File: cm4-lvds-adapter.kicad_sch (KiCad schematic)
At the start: 58 parts, among them J1 Plug_Molex_SlimStack_2x15_538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, J2 JST_SM_1x10_SM10B-SURS-TF-LF-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, J3 FFC_Amphenol_1x40_62684-40110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, U2 NTS0104_DHVQFN, U3 SN65DSI84

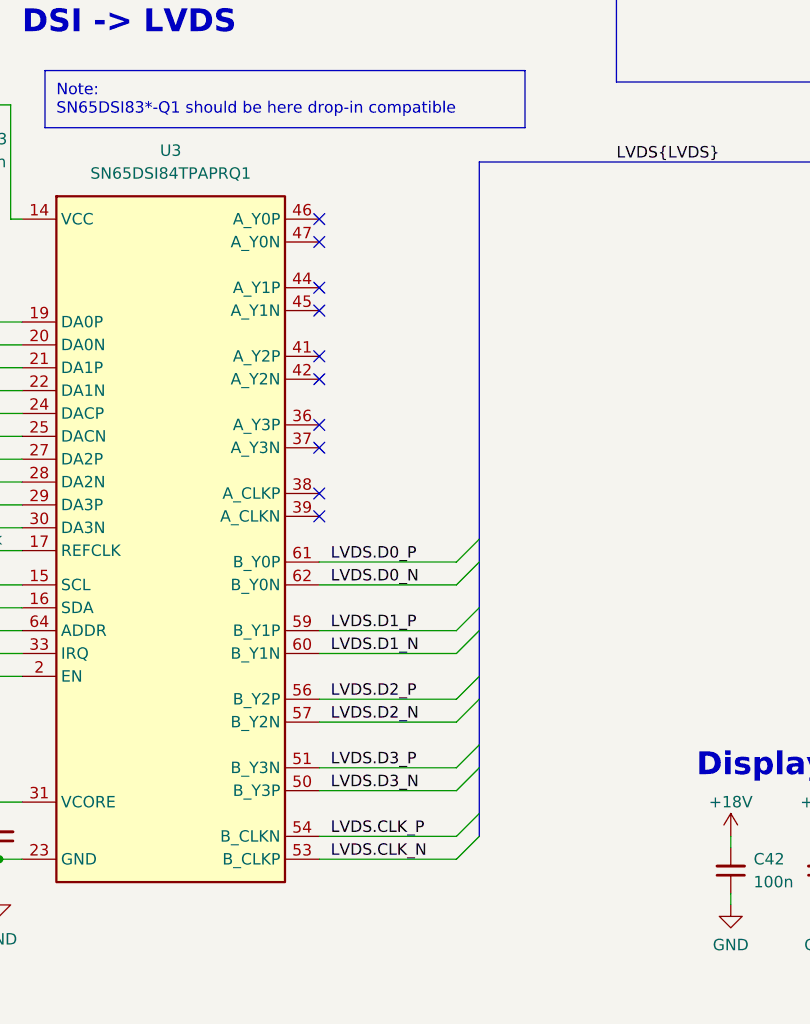
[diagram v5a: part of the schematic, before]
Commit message: [#55272] Correct pin assignment
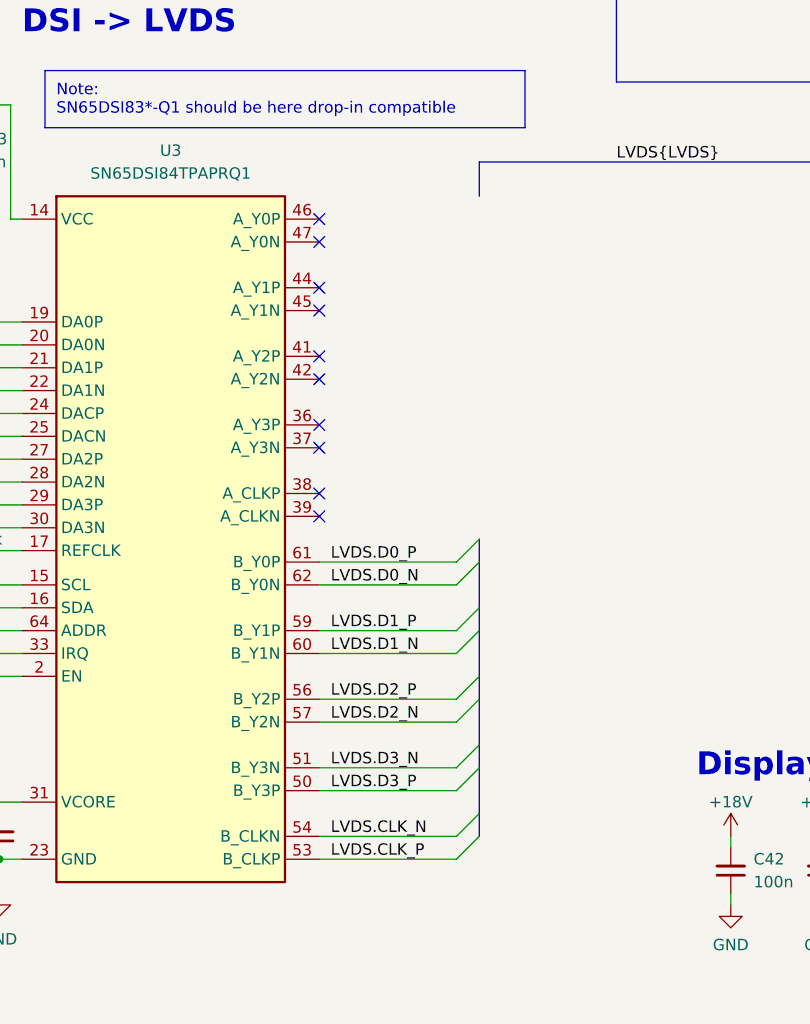
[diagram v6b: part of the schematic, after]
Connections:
- net LVDS.CLK_N: now also U3.54 (B_CLKN); no longer U3.53 (B_CLKP)
- net LVDS.CLK_P: now also U3.53 (B_CLKP); no longer U3.54 (B_CLKN)
- net LVDS.D3_N: now also U3.51 (B_Y3N); no longer U3.50 (B_Y3P)
- net LVDS.D3_P: now also U3.50 (B_Y3P); no longer U3.51 (B_Y3N)
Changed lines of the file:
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@@
     (stroke (width 0) (type default))
   )
-  (bus_entry (at 279.4 187.96) (size -2.54 2.54)
+  (bus_entry (at 279.4 185.42) (size -2.54 2.54)
     (stroke (width 0) (type default))
   )
@@
     (stroke (width 0) (type default))
   )
-  (bus_entry (at 279.4 185.42) (size -2.54 2.54)
+  (bus_entry (at 279.4 187.96) (size -2.54 2.54)
     (stroke (width 0) (type default))
   )
@@
     (stroke (width 0) (type default))
   )
+  (bus (pts (xy 279.4 185.42) (xy 279.4 187.96))
+    (stroke (width 0) (type default))
+  )
   (wire (pts (xy 100.33 189.23) (xy 120.65 189.23))
     (stroke (width 0) (type default))
@@
     (stroke (width 0) (type default))
   )
-  (bus (pts (xy 279.4 113.03) (xy 279.4 154.94))
+  (bus (pts (xy 279.4 113.03) (xy 279.4 116.84))
     (stroke (width 0) (type default))
   )
@@
     (stroke (width 0) (type default))
   )
-  (wire (pts (xy 261.62 187.96) (xy 276.86 187.96))
+  (wire (pts (xy 261.62 190.5) (xy 276.86 190.5))
     (stroke (width 0) (type default))
   )
@@
     (stroke (width 0) (type default))
   )
-  (wire (pts (xy 261.62 190.5) (xy 276.86 190.5))
+  (wire (pts (xy 261.62 187.96) (xy 276.86 187.96))
     (stroke (width 0) (type default))
   )
@@
     (stroke (width 0) (type default))
   )
-  (wire (pts (xy 261.62 182.88) (xy 276.86 182.88))
+  (wire (pts (xy 261.62 180.34) (xy 276.86 180.34))
     (stroke (width 0) (type default))
   )
@@
     (stroke (width 0) (type default))
   )
-  (bus (pts (xy 279.4 185.42) (xy 279.4 187.96))
-    (stroke (width 0) (type default))
-  )
   (wire (pts (xy 374.65 110.49) (xy 392.43 110.49))
     (stroke (width 0) (type default))
   )
-  (wire (pts (xy 261.62 180.34) (xy 276.86 180.34))
+  (wire (pts (xy 261.62 182.88) (xy 276.86 182.88))
     (stroke (width 0) (type default))
   )
@@
     (effects (font (size 1.27 1.27)) (justify right bottom))
   )
-  (label "LVDS.D3_P" (at 262.89 180.34 0) (fields_autoplaced)
+  (label "LVDS.D3_P" (at 262.89 182.88 0) (fields_autoplaced)
     (effects (font (size 1.27 1.27)) (justify left bottom))
   )
@@
     (effects (font (size 1.27 1.27)) (justify left bottom))
   )
-  (label "LVDS.CLK_P" (at 262.89 187.96 0) (fields_autoplaced)
+  (label "LVDS.CLK_P" (at 262.89 190.5 0) (fields_autoplaced)
     (effects (font (size 1.27 1.27)) (justify left bottom))
   )
@@
     (effects (font (size 1.27 1.27)) (justify right bottom))
   )
-  (label "LVDS.CLK_N" (at 262.89 190.5 0) (fields_autoplaced)
+  (label "LVDS.CLK_N" (at 262.89 187.96 0) (fields_autoplaced)
     (effects (font (size 1.27 1.27)) (justify left bottom))
   )
@@
     (effects (font (size 1.27 1.27)) (justify left bottom))
   )
-  (label "LVDS.D3_N" (at 262.89 182.88 0) (fields_autoplaced)
+  (label "LVDS.D3_N" (at 262.89 180.34 0) (fields_autoplaced)
     (effects (font (size 1.27 1.27)) (justify left bottom))
   )

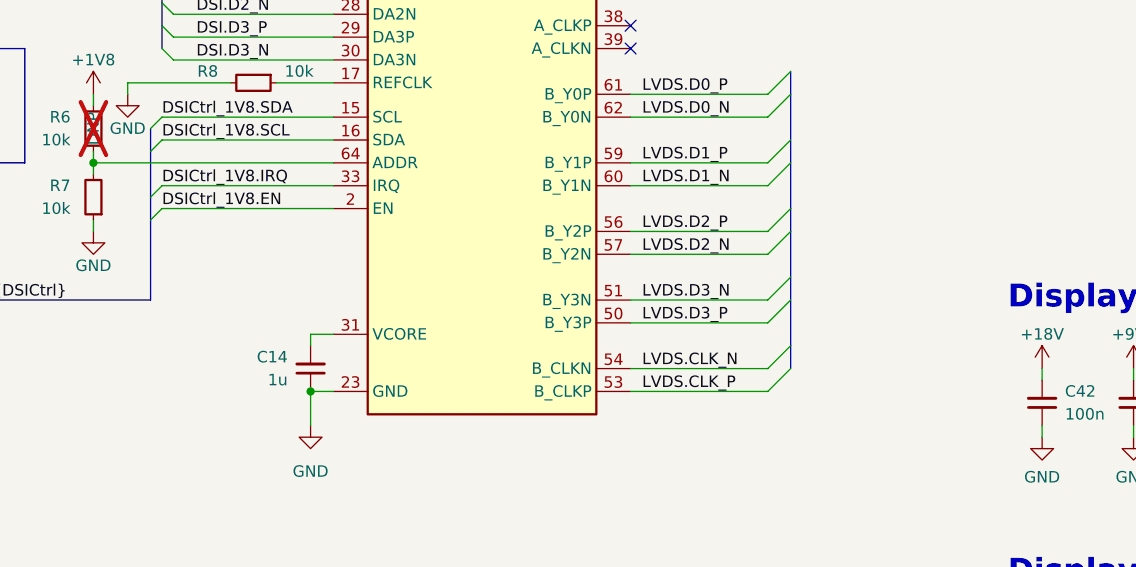
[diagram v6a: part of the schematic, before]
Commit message: [#55272] Update IRQ on the schematic
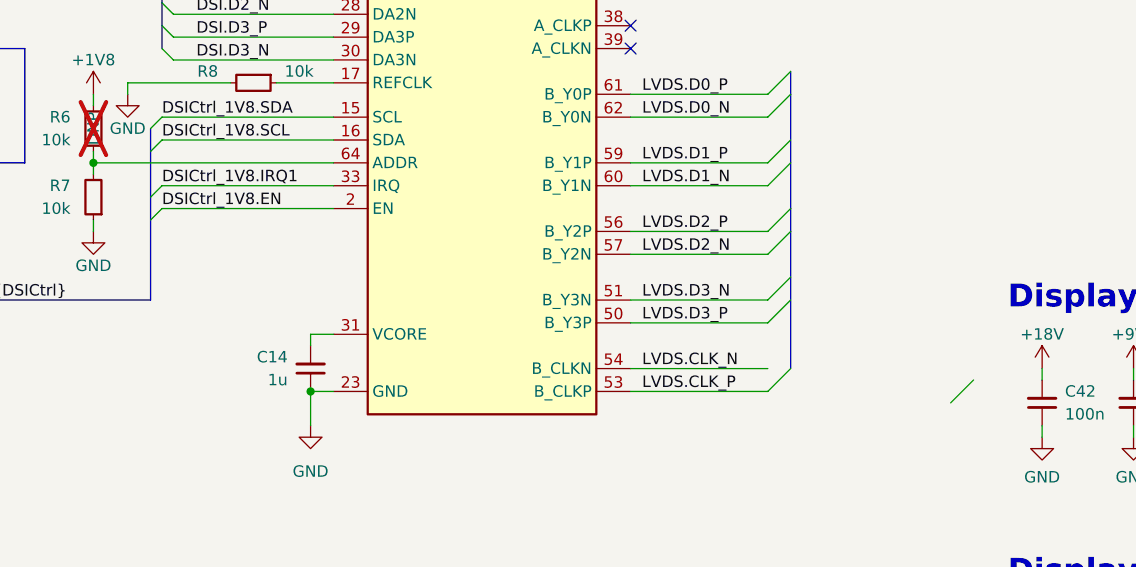
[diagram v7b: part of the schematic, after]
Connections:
- net DSICtrl_1V8.IRQ is gone; now on net DSICtrl_1V8.IRQ1: U3.33 (IRQ)
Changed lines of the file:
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@@
     (stroke (width 0) (type default))
   )
-  (bus_entry (at 279.4 185.42) (size -2.54 2.54)
+  (bus_entry (at 299.72 189.23) (size -2.54 2.54)
     (stroke (width 0) (type default))
   )
@@
     (stroke (width 0) (type default))
   )
-  (bus (pts (xy 279.4 185.42) (xy 279.4 187.96))
-    (stroke (width 0) (type default))
-  )
   (wire (pts (xy 100.33 189.23) (xy 120.65 189.23))
     (stroke (width 0) (type default))
@@
     (stroke (width 0) (type default))
   )
-  (bus (pts (xy 279.4 180.34) (xy 279.4 185.42))
+  (bus (pts (xy 279.4 180.34) (xy 279.4 187.96))
     (stroke (width 0) (type default))
   )
@@
     (effects (font (size 1.27 1.27)) (justify left bottom))
   )
-  (label "DSICtrl_1V8.IRQ" (at 209.55 167.64 0) (fields_autoplaced)
+  (label "DSICtrl_1V8.IRQ1" (at 209.55 167.64 0) (fields_autoplaced)
     (effects (font (size 1.27 1.27)) (justify left bottom))
   )

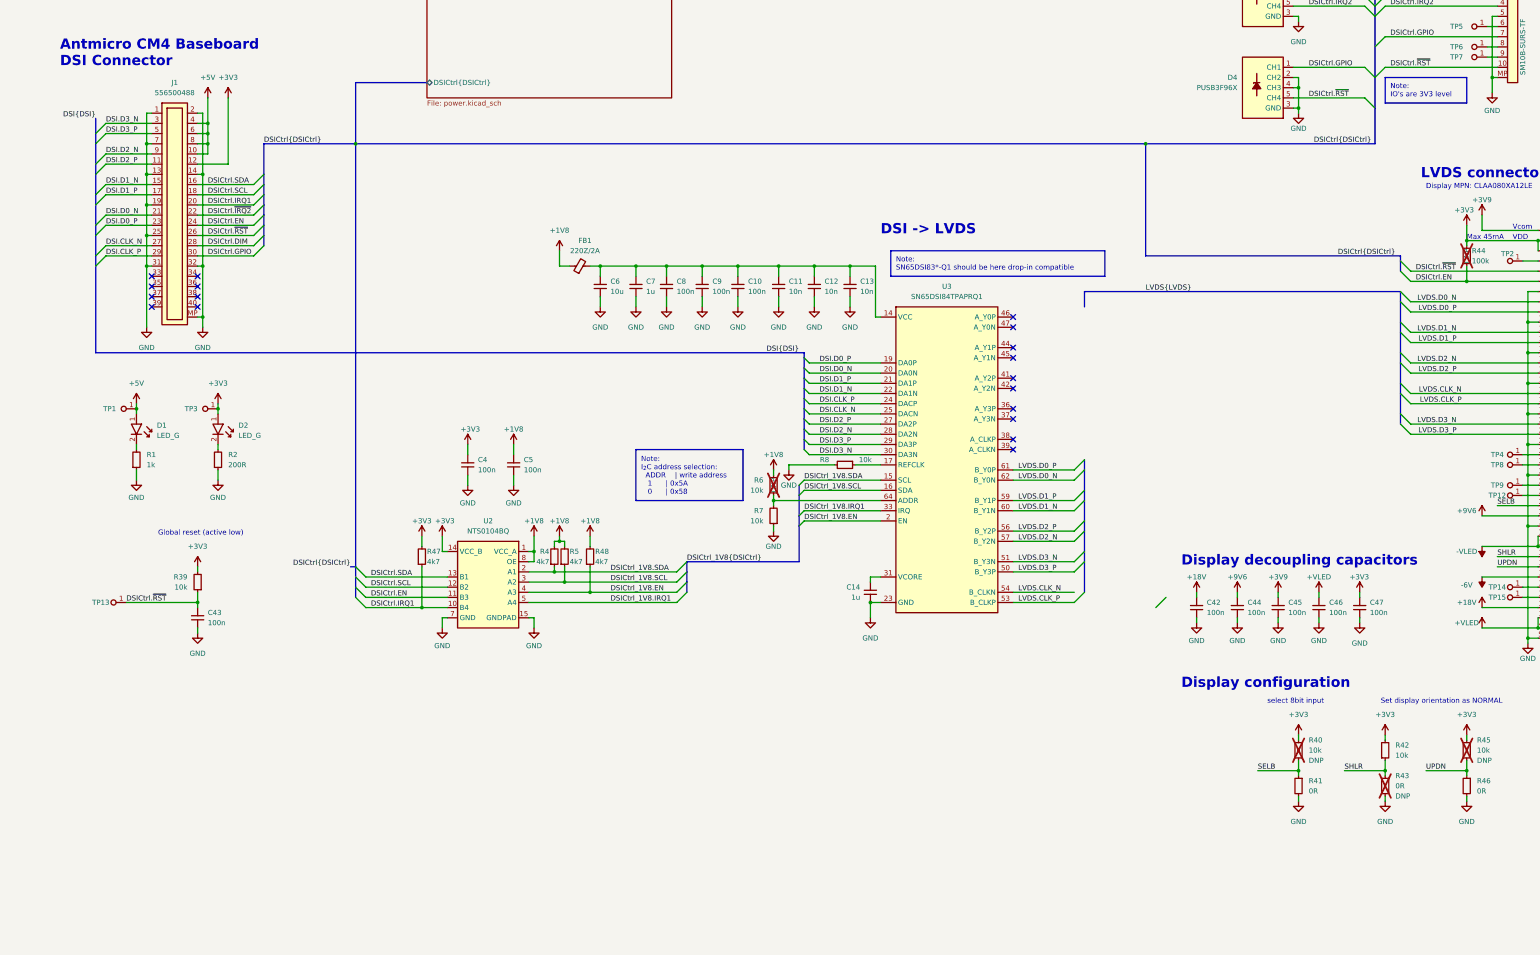
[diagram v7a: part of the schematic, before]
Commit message: [#55272] Route signals
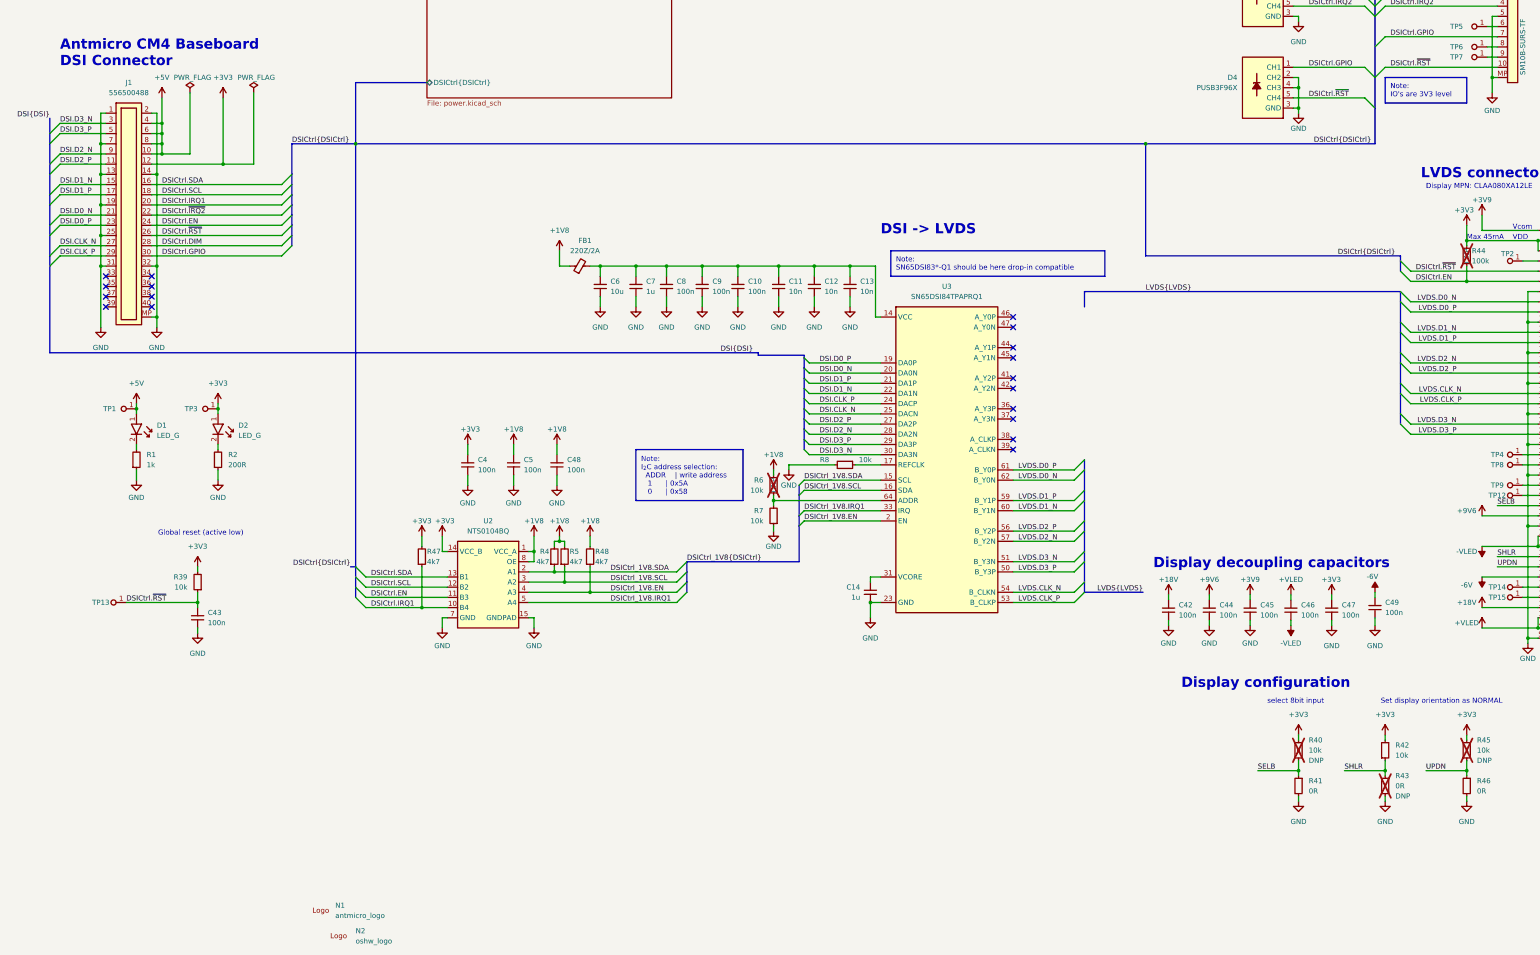
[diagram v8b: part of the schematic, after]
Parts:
- added C48, C49: C_100n_0402, antmicro-footprints:C_0402_1005Metric, symbol antmicroCapacitors0402:C_100n_0402
- added N1: antmicro_logo, antmicro-footprints:antmicro-logo_scaled_12mm, symbol antmicroMechanicalParts:antmicro_logo
- added N2: oshw_logo, antmicro-footprints:oshw-logo, symbol antmicroMechanicalParts:oshw_logo
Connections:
- net +1V8: now also C48.2
- net -6V: now also C49.2
- net -VLED: now also C46.1
- net GND: now also C48.1, C49.1; no longer C46.1
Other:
- moved on the sheet: C42, C44, C45, C46, C47, J1
